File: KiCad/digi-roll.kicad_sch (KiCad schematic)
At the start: 40 parts, among them Q1 PN2222A, SW1 SW_MEC_5E, SW2 SW_MEC_5E, SW3 SW_MEC_5E, SW4 SW_MEC_5E, SW5 SW_MEC_5E, SW6 SW_MEC_5E, SW7 SW_MEC_5E, SW8 SW_MEC_5E, SW9 SW_DPST_x2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

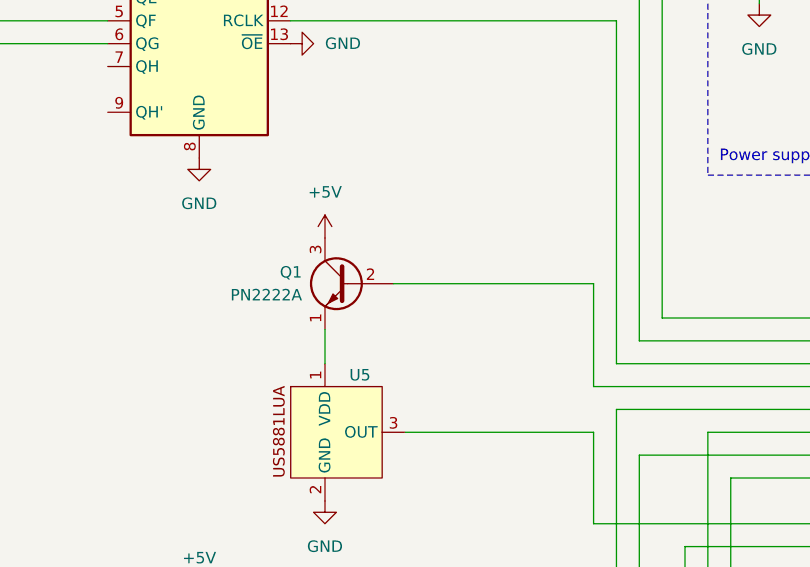
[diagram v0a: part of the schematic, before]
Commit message: remove BPJ for HALL
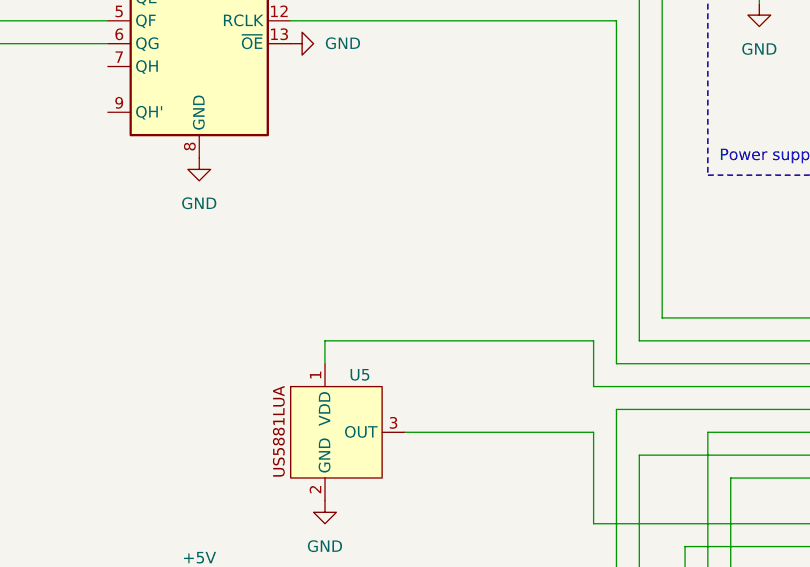
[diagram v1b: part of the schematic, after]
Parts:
- removed Q1: PN2222A, Package_TO_SOT_THT:TO-92_Inline, symbol Transistor_BJT:PN2222A
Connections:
- net at U5.1 (VDD): now also U1.10 (PA3)
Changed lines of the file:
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@@
-    (stroke (width 0) (type default))
-  )
-  (wire (pts (xy 93.98 74.93) (xy 93.98 78.74))
     (stroke (width 0) (type default))
   )
@@
   )
   (wire (pts (xy 67.31 127) (xy 67.31 189.23))
+    (stroke (width 0) (type default))
+  )
+  (wire (pts (xy 93.98 76.2) (xy 123.825 76.2))
     (stroke (width 0) (type default))
   )
@@
     (stroke (width 0) (type dash) (color 132 0 0 1))
   )
-  (wire (pts (xy 123.825 81.28) (xy 123.825 69.85))
+  (wire (pts (xy 123.825 81.28) (xy 123.825 76.2))
     (stroke (width 0) (type default))
   )
@@
   )
   (wire (pts (xy 151.765 96.52) (xy 123.825 96.52))
-    (stroke (width 0) (type default))
-  )
-  (wire (pts (xy 123.825 69.85) (xy 101.6 69.85))
     (stroke (width 0) (type default))
   )
@@
   )
   (wire (pts (xy 170.815 43.18) (xy 170.815 38.735))
+    (stroke (width 0) (type default))
+  )
+  (wire (pts (xy 93.98 76.2) (xy 93.98 78.74))
     (stroke (width 0) (type default))
   )
@@
     )
   )
-  (symbol (lib_id "Transistor_BJT:PN2222A") (at 96.52 69.85 0) (mirror y) (unit 1)
-    (in_bom yes) (on_board yes) (dnp no)
-    (property "Reference" "Q1" (at 91.44 68.58 0)
-      (effects (font (size 1.27 1.27)) (justify left))
-    )
-    (property "Value" "PN2222A" (at 91.44 71.12 0)
-      (effects (font (size 1.27 1.27)) (justify left))
-    )
-    (property "Footprint" "Package_TO_SOT_THT:TO-92_Inline" (at 91.44 71.755 0)
-      (effects (font (size 1.27 1.27) italic) (justify left) hide)
-    )
-    (property "Datasheet" "https://www.onsemi.com/pub/Collateral/PN2222-D.PDF" (at 96.52 69.85 0)
-      (effects (font (size 1.27 1.27)) (justify left) hide)
-    )
-    (pin "1")
-    (pin "2")
-    (pin "3")
-    (instances
-      (project "digi-roll"
-        (path "/09ea68d6-8698-4f00-9100-69fad1a7bee2"
-          (reference "Q1") (unit 1)
-        )
-      )
-    )
-  )
   (symbol (lib_id "Device:R_US") (at 30.48 78.74 270) (mirror x) (unit 1)
     (in_bom yes) (on_board yes) (dnp no) (fields_autoplaced)
@@
         )
       )
-    )
-  )
-  (symbol (lib_id "power:+5V") (at 93.98 64.77 0) (unit 1)
-    (in_bom yes) (on_board yes) (dnp no) (fields_autoplaced)
-    (property "Reference" "#PWR06" (at 93.98 68.58 0)
-      (effects (font (size 1.27 1.27)) hide)
-    )
-    (property "Value" "+5V" (at 93.98 59.69 0)
-      (effects (font (size 1.27 1.27)))
-    )
-    (property "Footprint" "" (at 93.98 64.77 0)
-      (effects (font (size 1.27 1.27)) hide)
-    )
-    (property "Datasheet" "" (at 93.98 64.77 0)
-      (effects (font (size 1.27 1.27)) hide)
-    )
-    (pin "1")
-    (instances
-      (project "digi-roll"
-        (path "/09ea68d6-8698-4f00-9100-69fad1a7bee2"
-          (reference "#PWR06") (unit 1)
-        )
-      )

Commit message: finish PCB order
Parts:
- added C2: 0.1µF, Capacitor_THT:C_Disc_D4.7mm_W2.5mm_P5.00mm, symbol Device:C
- added J1: AVR-ISP-6, Connector_PinHeader_2.54mm:PinHeader_2x03_P2.54mm_Vertical, symbol Connector:AVR-ISP-6
- BT1, SW9: footprint (none) -> Connector_PinHeader_2.54mm:PinHeader_1x02_P2.54mm_Vertical
- C1: footprint (none) -> Capacitor_THT:C_Disc_D4.7mm_W2.5mm_P5.00mm
- D1, D2, D3, D4, D5, D6, D7: footprint (none) -> LED_THT:LED_D5.0mm
- R1, R10, R11, R12, R13, R14, R15, R2, R3, R4, R5, R6, R7, R8, R9: footprint (none) -> Resistor_THT:R_Axial_DIN0207_L6.3mm_D2.5mm_P7.62mm_Horizontal
- SW1, SW2, SW3, SW4, SW5, SW6, SW7, SW8: footprint (none) -> Button_Switch_THT:SW_PUSH_6mm_H5mm; symbol Switch:SW_MEC_5E -> Switch:SW_Push
- U2, U3: footprint (none) -> Package_DIP:DIP-16_W7.62mm
- U4: footprint (none) -> Zane:Adafruit_7_seg
- U5: footprint (none) -> Connector_PinHeader_2.54mm:PinHeader_1x03_P2.54mm_Vertical
- U6: footprint (none) -> Zane:Adafruit_Miniboost
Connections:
- net +5V: now also C2.1; no longer SW1.2, SW2.2, SW3.2, SW4.2, SW5.2, SW6.2, SW7.2, SW8.2
- net GND: now also C2.2, J1.6 (GND)
- net at R10.1: now also SW3.2, U3.2 (D5); no longer SW3.4 (A)
- net at R15.1: now also SW8.2, U3.10 (D0); no longer SW8.4 (A)
- net at U1.9 (PA4), U4.26 (SCL): now also J1.3 (SCK)
- net at U1.7 (PA6), U4.27 (SDA): now also J1.4 (MOSI)
- net at R12.1: now also SW5.2, U3.13 (D3); no longer SW5.4 (A)
- net at R14.1: now also SW7.2, U3.11 (D1); no longer SW7.4 (A)
- net at U3.1 (D4): now also R11.1, SW4.2; no longer SW4.3 (K)
- net at U3.12 (D2): now also R13.1, SW6.2; no longer SW6.3 (K)
- net at U3.3 (D6): now also R9.1, SW2.2; no longer SW2.3 (K)
- net at U3.4 (D7): now also R8.1, SW1.2; no longer SW1.3 (K)
- net at U1.8 (PA5), U3.9 (Q0): now also J1.1 (MISO)
- net at SW9.2 (B), U6.1 (VIN): now also J1.2 (VCC)
- net at U1.4 (~{RESET}/PB3): now also J1.5 (~{RST})
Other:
- moved on the sheet: C1, U4, U5
